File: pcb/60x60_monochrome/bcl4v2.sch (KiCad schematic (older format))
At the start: 30 parts, among them Q1 BSS138, SW1 SW_Push, SW2 SW_Push, SW3 SW_Push, U1 DS9166A-23, U2 STM32F070CBTx, Y1 Resonator

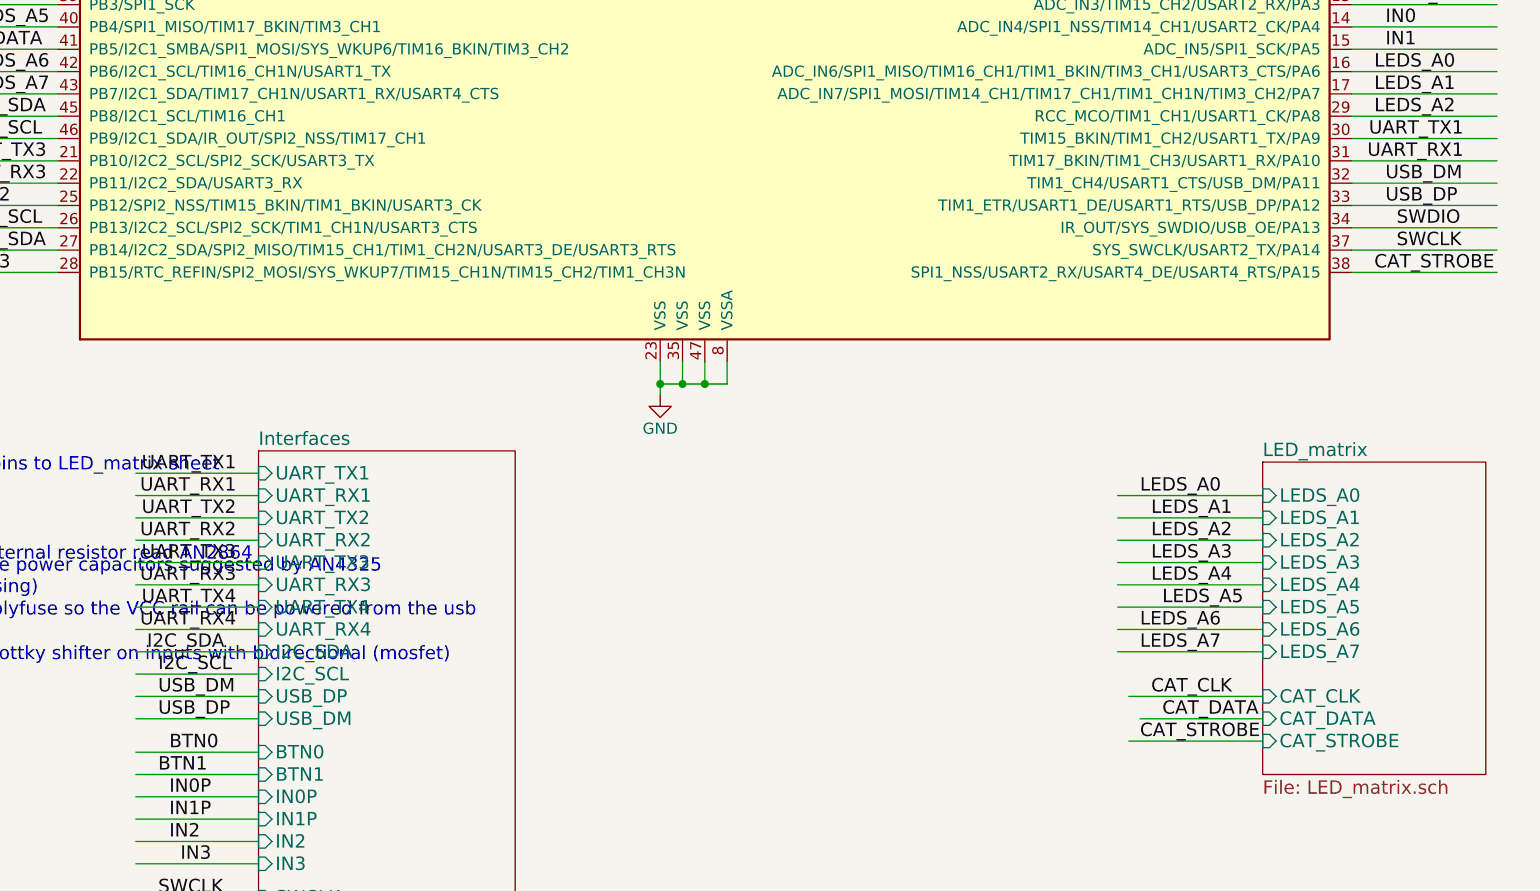
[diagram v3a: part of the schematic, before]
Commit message: - fix USB lines
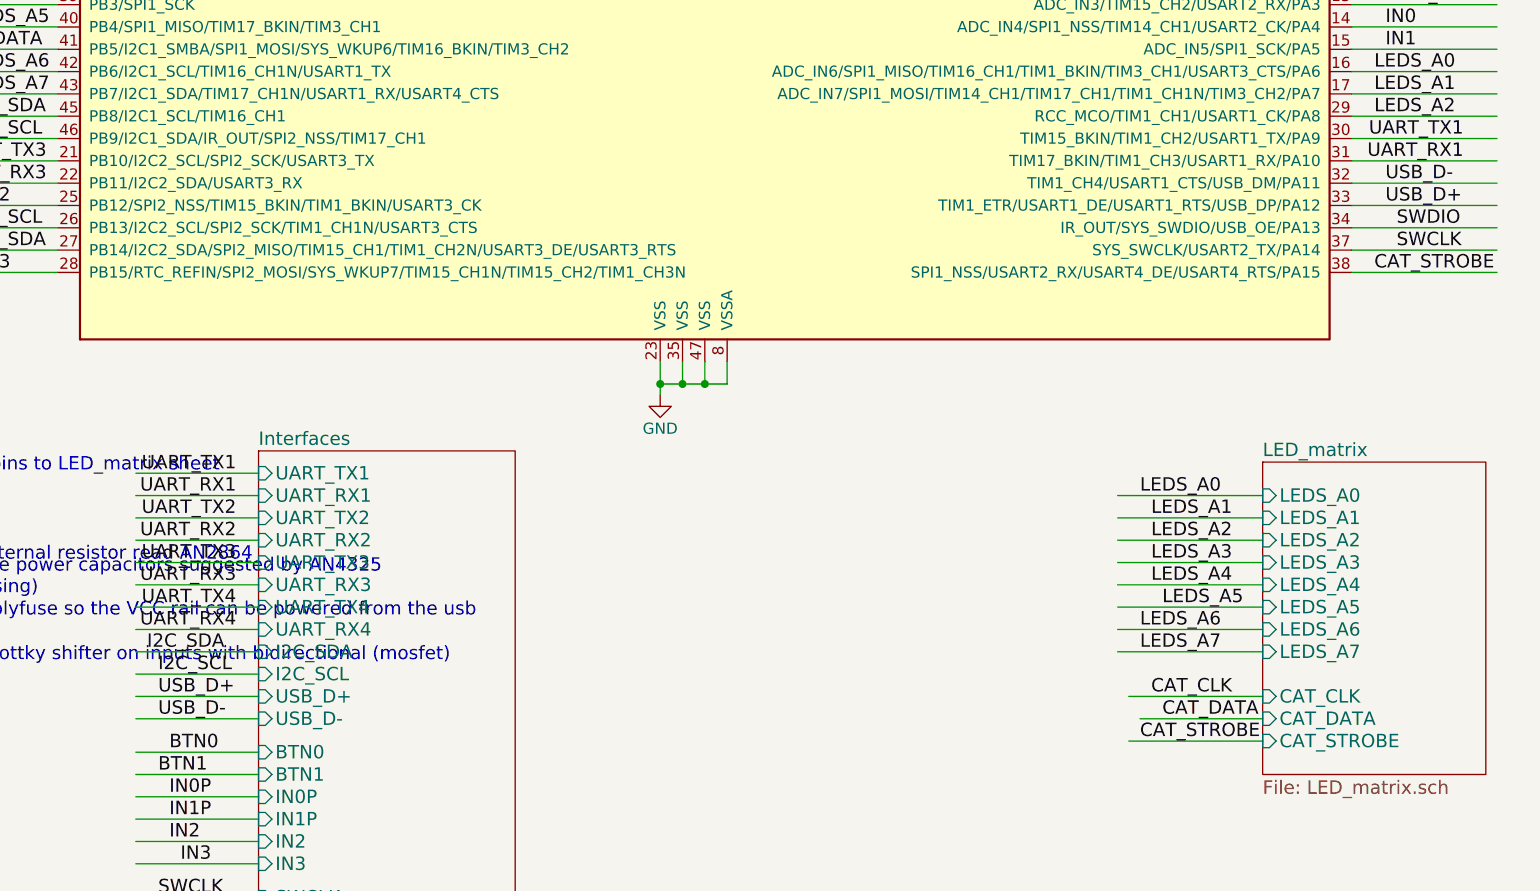
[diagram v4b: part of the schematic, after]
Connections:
- net labels added: USB_D+, USB_D-
- net labels removed: USB_DM, USB_DP
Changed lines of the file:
@@
 LIBS:contrib
 LIBS:valves
-LIBS:badger_ir2301
-LIBS:badger_mosfet_sot669
-LIBS:badger_zxct1110
 LIBS:stm32
 LIBS:74xgxx
@@
 LIBS:Xicor
 LIBS:Zilog
-LIBS:badger_dualmosfet_DMC2038LVT
-LIBS:wt51822-s4at
-LIBS:badger_resonator
-LIBS:LED_MATRIX_ysm-2388crgbc
-LIBS:badger_dm163_LED_DRIVER
-LIBS:badger_led_matrix_8x8
-LIBS:badger_m54564fp
-LIBS:badger_npic6c595
 LIBS:bcl4v2-cache
 EELAYER 25 0
@@
 LEDS_A7
 Text Label 10550 3750 0    60   ~ 0
-USB_DM
+USB_D-
 Text Label 10550 3850 0    60   ~ 0
-USB_DP
+USB_D+
 Text Label 4200 3950 0    60   ~ 0
 I2C_SCL
@@
 F10 "I2C_SDA" I L 5500 5850 60
 F11 "I2C_SCL" I L 5500 5950 60
-F12 "USB_DM" I L 5500 6150 60
-F13 "USB_DP" I L 5500 6050 60
+F12 "USB_D-" I L 5500 6150 60
+F13 "USB_D+" I L 5500 6050 60
 F14 "BOOT0" I L 5500 7300 60
 F15 "NRST" I L 5500 7150 60
@@
 Text Label 5000 5850 0    60   ~ 0
 I2C_SDA
+Text Label 5050 6150 0    60   ~ 0
+USB_D-
 Text Label 5050 6050 0    60   ~ 0
-USB_DM
-Text Label 5050 6150 0    60   ~ 0
-USB_DP
+USB_D+
 Wire Wire Line
 	5500 6050 4950 6050
